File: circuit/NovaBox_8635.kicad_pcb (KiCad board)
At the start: 2 copper layers, 82 x 30 mm, 86 parts, among them P1 MH, P2 MH, P3 MH, P4 MH, P5 USB, Q1 MMBT3904, Q2 IRLML6344, Q3 IRLML6401, Q4 MMBT3904, Q5 MMBT3904, SW1 PIO18, SW2 PIO21, SW3 PIO8, SW4 PIO0, SW5 PIO1, SW6 ON/OFF, U1 MCP6004, U2 CSR8635_MODULE, U3 CSR_DebugSmall, U4 PAM8304, U5 PAM8304, U6 LT1308

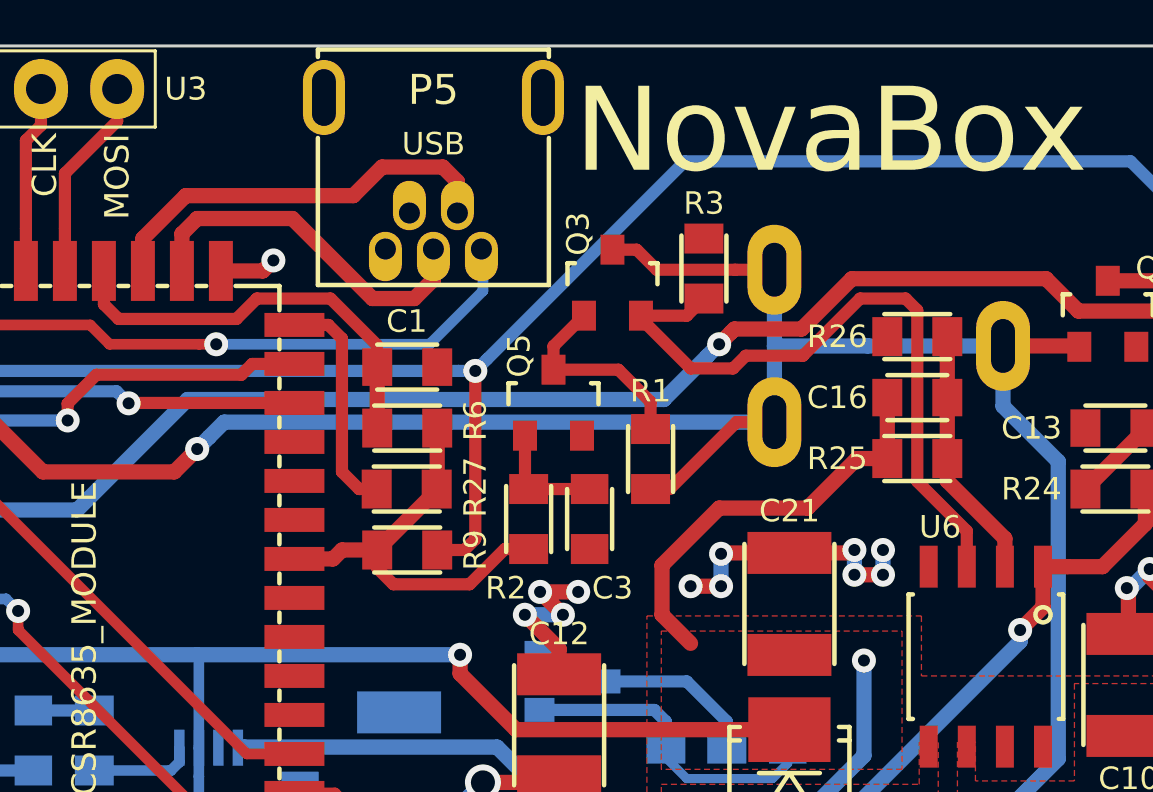
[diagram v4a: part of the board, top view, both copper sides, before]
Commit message: removed C3 on base of NPN
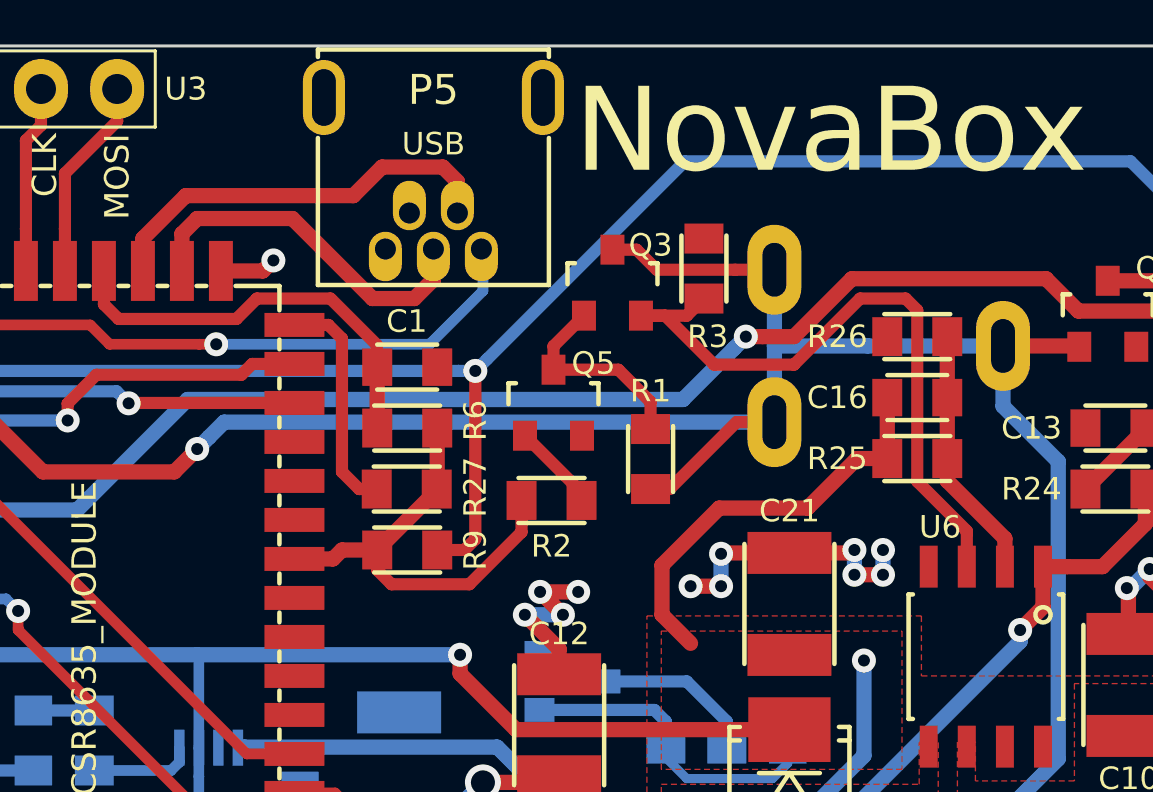
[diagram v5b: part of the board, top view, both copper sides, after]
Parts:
- removed C3: 1uF, NovaBox:C_0805
- moved R2 0.98 mm to (115.6, 65.2), turned to 180 degrees
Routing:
- net 1V8: track 14.3 -> 15.4 mm
- net Net-(C3-Pad2): track 3.86 -> 2.94 mm

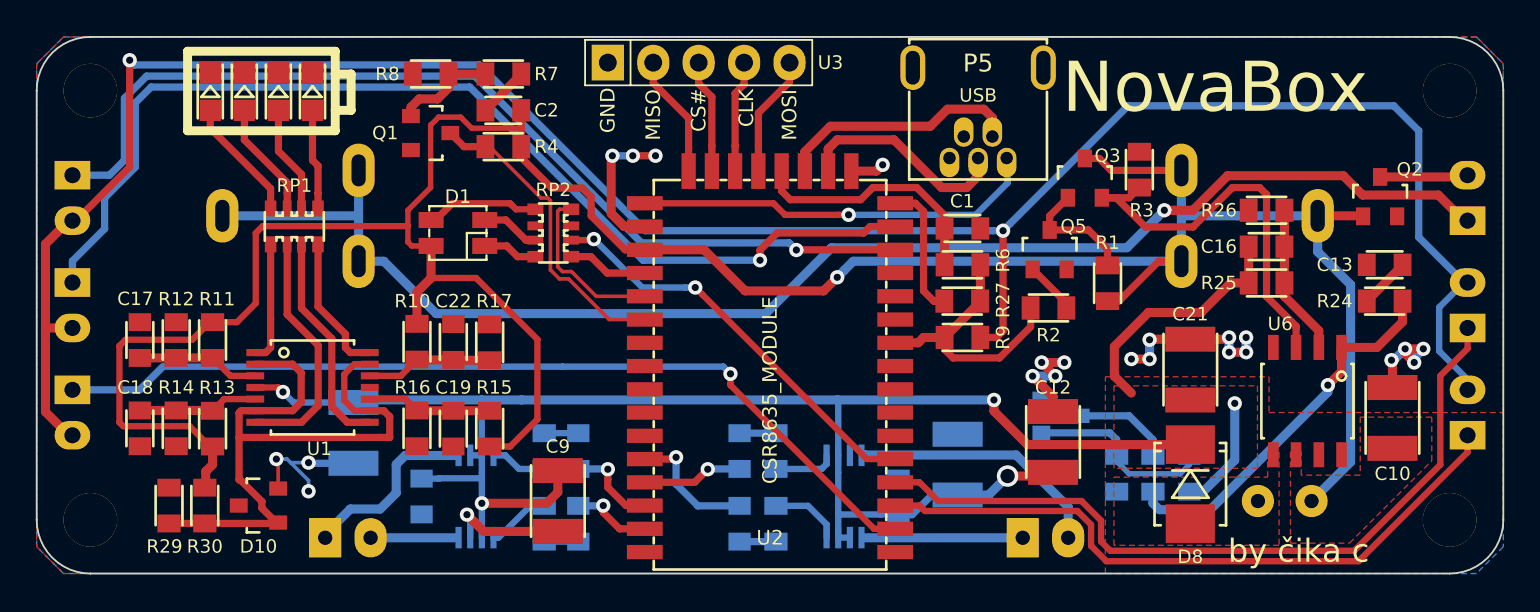
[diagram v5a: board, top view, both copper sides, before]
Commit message: added reverse battery indicator
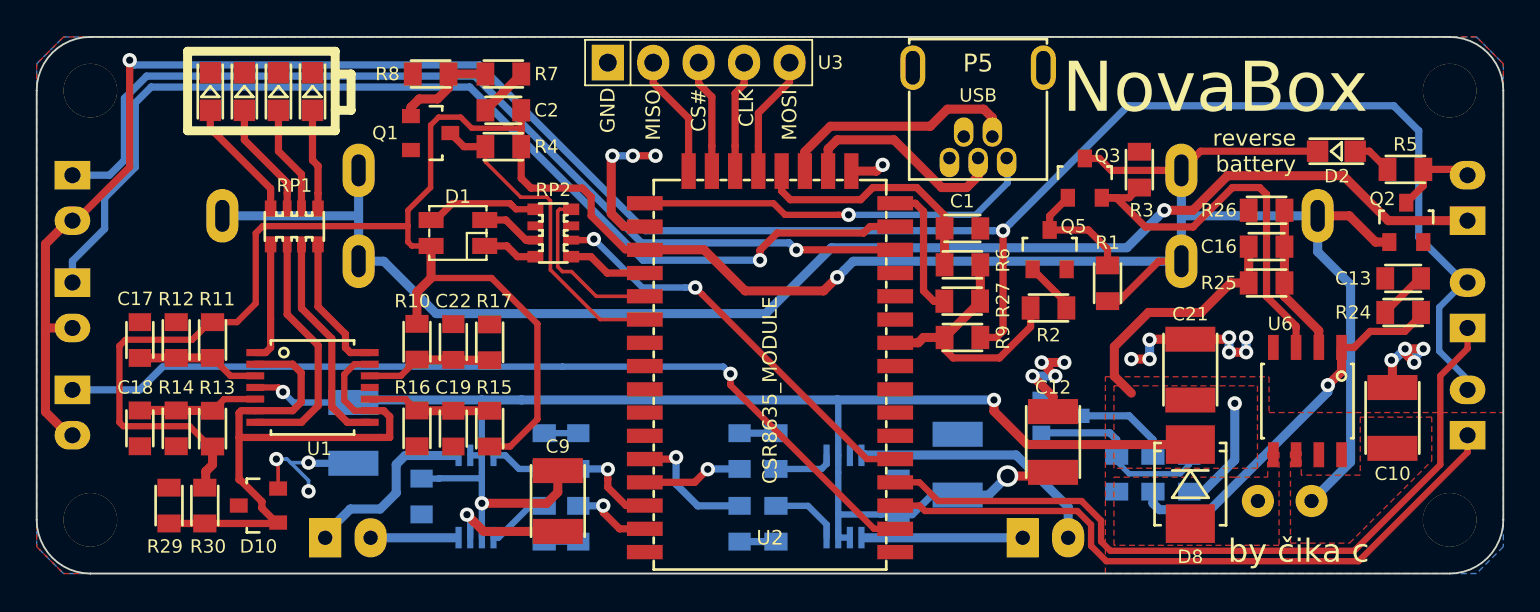
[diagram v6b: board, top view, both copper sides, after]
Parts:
- added D2: REVERSE_BATT, NovaBox:LED_0805, F.Cu at (131.7, 56.4)
- added R5: 1K, NovaBox:R_0805, F.Cu at (135.5, 57.4)
- moved Q2 2.05 mm to (135.6, 60.4)
- moved C13 1.28 mm to (135.4, 63.5)
- moved R24 1.21 mm to (135.4, 65.4)
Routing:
- net +BATT: track 155.5 -> 166.8 mm
- net Net-(D2-Pad2): track 0.00 -> 2.23 mm
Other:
- board text added: "reverse battery"

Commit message: calculated voltage dividers for battey charge level
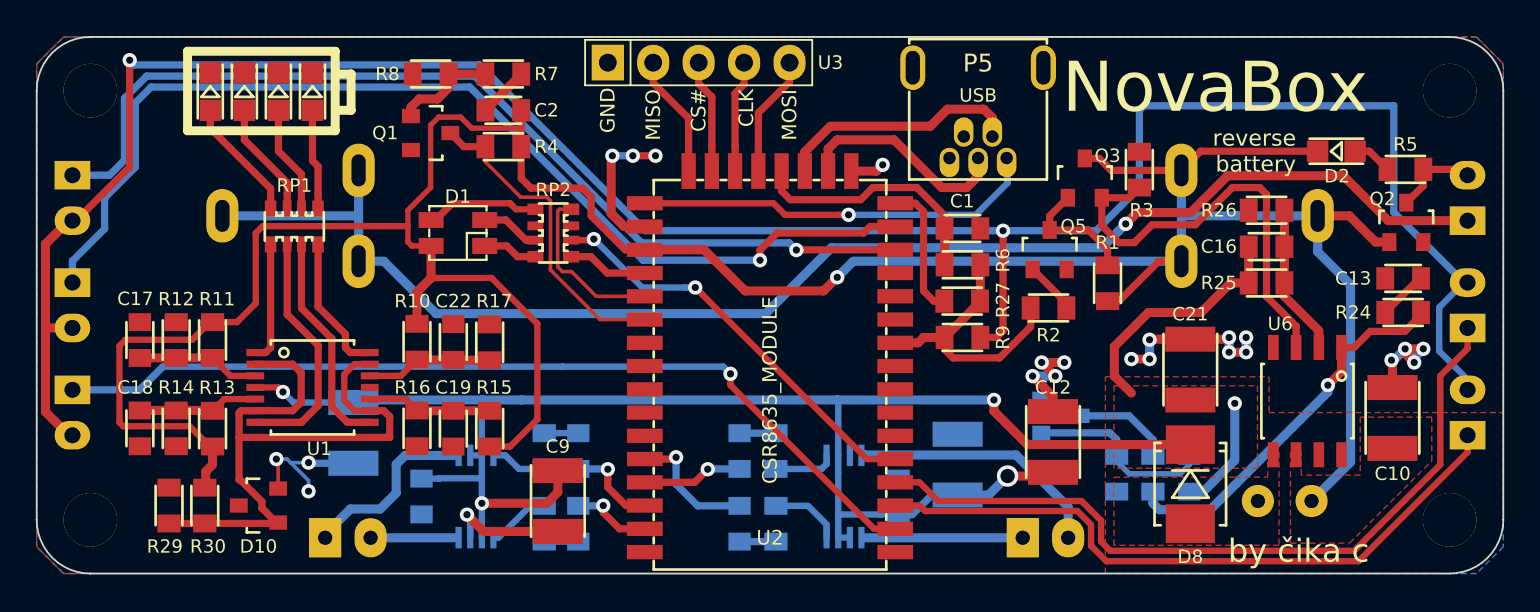
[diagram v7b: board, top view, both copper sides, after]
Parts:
- C17, C18, C19, C22: value 100nF -> 1uF
- D4: value BATT_H -> BATT_E
- D5: value BATT_M -> BATT_L
- D6: value BATT_L -> BATT_M
- D7: value BATT_E -> BATT_H
- R10: value 180K -> 270K
- R11: value 270K -> 240K
- R12, R14: value 510K -> 620K
- R13: value 220K -> 270K
- R15: value 180K -> 240K
- R16, R17: value 510K -> 470K
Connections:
- net BTLN renamed Net-(R20-Pad2)
- net BTLP renamed Net-(R18-Pad2)
- net BTRN renamed Net-(R21-Pad2)
- net BTRP renamed Net-(R19-Pad2)
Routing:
- net Net-(R9-Pad2): track 129.5 -> 132.0 mm
- net VR_SHDN: track 22.5 -> 24.2 mm

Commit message: updated PDF and date on PCB
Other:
- board text added: "2018.aug.19"
- board text removed: "2018.aug.13"
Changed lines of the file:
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@@
   (gr_arc (start 62 77) (end 62 80) (angle 90) (layer Edge.Cuts) (width 0.1))
   (gr_arc (start 62 53) (end 59 53) (angle 90) (layer Edge.Cuts) (width 0.1))
-  (gr_text 2018.aug.13 (at 75.946 52.705 180) (layer B.SilkS)
+  (gr_text 2018.aug.19 (at 75.946 52.705 180) (layer B.SilkS)
     (effects (font (size 1.5 1.5) (thickness 0.3)) (justify mirror))
   )
@@
   (segment (start 109.1565 64.77) (end 109.744 64.77) (width 0.4064) (layer F.Cu) (net 41) (status 20))
   (segment (start 108.585 64.1985) (end 109.1565 64.77) (width 0.4064) (layer F.Cu) (net 41))
-  (segment (start 84.541 77.992) (end 84.822 77.992) (width 0.3556) (layer B.Cu) (net 66) (status 10))
-  (segment (start 84.822 77.992) (end 86.598 76.216) (width 0.3556) (layer B.Cu) (net 66))
-  (segment (start 86.598 76.216) (end 87.376 76.216) (width 0.3556) (layer B.Cu) (net 66) (status 20))
-  (segment (start 103.165 73.392) (end 103.165 73.873) (width 0.3556) (layer B.Cu) (net 67) (status 30))
-  (segment (start 103.165 73.873) (end 102.886 74.152) (width 0.3556) (layer B.Cu) (net 67) (status 10))
-  (segment (start 102.886 74.152) (end 100.076 74.152) (width 0.3556) (layer B.Cu) (net 67) (status 20))
-  (segment (start 84.541 73.392) (end 85.203 73.392) (width 0.3556) (layer B.Cu) (net 68) (status 10))
-  (segment (start 85.203 73.392) (end 85.963 74.152) (width 0.3556) (layer B.Cu) (net 68))
-  (segment (start 85.963 74.152) (end 87.376 74.152) (width 0.3556) (layer B.Cu) (net 68) (status 20))
-  (segment (start 100.076 76.216) (end 102.124 76.216) (width 0.3556) (layer B.Cu) (net 69) (status 10))
-  (segment (start 102.124 76.216) (end 103.165 77.257) (width 0.3556) (layer B.Cu) (net 69))
-  (segment (start 103.165 77.257) (end 103.165 77.992) (width 0.3556) (layer B.Cu) (net 69) (status 20))
   (segment (start 64.77 67.945) (end 66.802 67.945) (width 0.508) (layer F.Cu) (net 42) (status 30))
   (segment (start 68.834 67.945) (end 66.802 67.945) (width 0.508) (layer F.Cu) (net 42) (status 30))
@@
   (segment (start 116.57 64.876) (end 114.686 62.992) (width 0.4064) (layer F.Cu) (net 65))
   (segment (start 116.57 65.151) (end 116.57 64.876) (width 0.4064) (layer F.Cu) (net 65))
+  (segment (start 84.541 77.992) (end 84.822 77.992) (width 0.3556) (layer B.Cu) (net 66) (status 10))
+  (segment (start 84.822 77.992) (end 86.598 76.216) (width 0.3556) (layer B.Cu) (net 66))
+  (segment (start 86.598 76.216) (end 87.376 76.216) (width 0.3556) (layer B.Cu) (net 66) (status 20))
+  (segment (start 103.165 73.392) (end 103.165 73.873) (width 0.3556) (layer B.Cu) (net 67) (status 30))
+  (segment (start 103.165 73.873) (end 102.886 74.152) (width 0.3556) (layer B.Cu) (net 67) (status 10))
+  (segment (start 102.886 74.152) (end 100.076 74.152) (width 0.3556) (layer B.Cu) (net 67) (status 20))
+  (segment (start 84.541 73.392) (end 85.203 73.392) (width 0.3556) (layer B.Cu) (net 68) (status 10))
+  (segment (start 85.203 73.392) (end 85.963 74.152) (width 0.3556) (layer B.Cu) (net 68))
+  (segment (start 85.963 74.152) (end 87.376 74.152) (width 0.3556) (layer B.Cu) (net 68) (status 20))
+  (segment (start 100.076 76.216) (end 102.124 76.216) (width 0.3556) (layer B.Cu) (net 69) (status 10))
+  (segment (start 102.124 76.216) (end 103.165 77.257) (width 0.3556) (layer B.Cu) (net 69))
+  (segment (start 103.165 77.257) (end 103.165 77.992) (width 0.3556) (layer B.Cu) (net 69) (status 20))
   (zone (net 0) (net_name "") (layer B.Cu) (hatch edge 0.508)
     (connect_pads (clearance 0.254))
